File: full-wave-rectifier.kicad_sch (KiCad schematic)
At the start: 40 parts, among them J10 Control Right, J11 Main Right, J2 Input Ch1, J3 Input Ch2, J4 Output Ch1, J5 Output Ch2, J6 Ochd input, J8 Control Left, J9 Main Left, U2 TL074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

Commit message: Updated control panel
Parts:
- R10, R11, R12, R13, R14, R15, R16, R17, R18, R19, R20, R3, R4, R9: value 100k_TH0.125 -> 100k
- R21, R22: value 51k_TH0.125 -> 51k
- R5, R6, R7, R8: value 1k_TH0.125 -> 1k
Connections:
- net GND: now also J10.1 (Pin_1), J10.8 (Pin_8), J11.1 (Pin_1), J11.8 (Pin_8), J8.1 (Pin_1), J8.8 (Pin_8), J9.1 (Pin_1), J9.8 (Pin_8); no longer J10.4 (Pin_4), J10.6 (Pin_6), J11.4 (Pin_4), J11.6 (Pin_6), J8.4 (Pin_4), J8.6 (Pin_6), J9.4 (Pin_4), J9.6 (Pin_6)
- removed net AMP_CH1: AMP_CH1.1, J8.1 (Pin_1), J9.1 (Pin_1), R19.2, U4.7
- removed net AMP_CH2: AMP_CH2.1, J10.2 (Pin_2), J11.2 (Pin_2), R20.2, U4.8
- removed net INPUT_CH1: J8.7 (Pin_7), J9.7 (Pin_7), R5.2, U3.3 (+)
- removed net INPUT_CH2: J10.7 (Pin_7), J11.7 (Pin_7), R6.2, U3.12 (+)
- removed net OFFSET_CH1: J8.3 (Pin_3), J9.3 (Pin_3), OFFSET_CH1.1, U2.1, U2.2 (-)
- removed net OFFSET_CH2: J10.1 (Pin_1), J11.1 (Pin_1), OFFSET_CH2.1, U2.13 (-), U2.14
- removed net OUTPUT_CH1: J8.8 (Pin_8), J9.8 (Pin_8), R7.1, U3.6 (-), U3.7
- removed net OUTPUT_CH2: J10.8 (Pin_8), J11.8 (Pin_8), R8.1, U3.8, U3.9 (-)
- removed net SUM_CH1: J8.2 (Pin_2), J9.2 (Pin_2), R10.1, R9.2, U3.5 (+)
- removed net SUM_CH2: J10.3 (Pin_3), J11.3 (Pin_3), R11.2, R12.1, U3.10 (+)
- new net M_AMP_CH1: J9.3 (Pin_3), R19.2, U4.7
- new net M_AMP_CH2: J11.3 (Pin_3), R20.2, U4.8
- new net M_INPUT_CH1: J9.2 (Pin_2), U3.3 (+)
- new net M_INPUT_CH2: J11.2 (Pin_2), U3.12 (+)
- new net M_OFFSET_CH1: J9.6 (Pin_6), U2.1, U2.2 (-)
- new net M_OFFSET_CH2: J11.4 (Pin_4), U2.13 (-), U2.14
- new net M_OUTPUT_CH1: J9.7 (Pin_7), U3.6 (-), U3.7
- new net M_OUTPUT_CH2: J11.7 (Pin_7), U3.8, U3.9 (-)
- new net M_SUM_CH1: J9.4 (Pin_4), U3.5 (+)
- new net M_SUM_CH2: J11.6 (Pin_6), U3.10 (+)
- new net С_AMP_CH1: AMP_CH1.1, J8.3 (Pin_3)
- new net С_AMP_CH2: AMP_CH2.1, J10.3 (Pin_3)
- new net С_INPUT_CH1: J8.2 (Pin_2), R5.2
- new net С_INPUT_CH2: J10.2 (Pin_2), R6.2
- new net С_OFFSET_CH1: J8.6 (Pin_6), OFFSET_CH1.1
- new net С_OFFSET_CH2: J10.4 (Pin_4), OFFSET_CH2.1
- new net С_OUTPUT_CH1: J8.7 (Pin_7), R7.1
- new net С_OUTPUT_CH2: J10.7 (Pin_7), R8.1
- new net С_SUM_CH1: J8.4 (Pin_4), R10.1, R9.2
- new net С_SUM_CH2: J10.6 (Pin_6), R11.2, R12.1
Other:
- moved on the sheet: J10, J11, J6, J8, J9, U2B, U2C

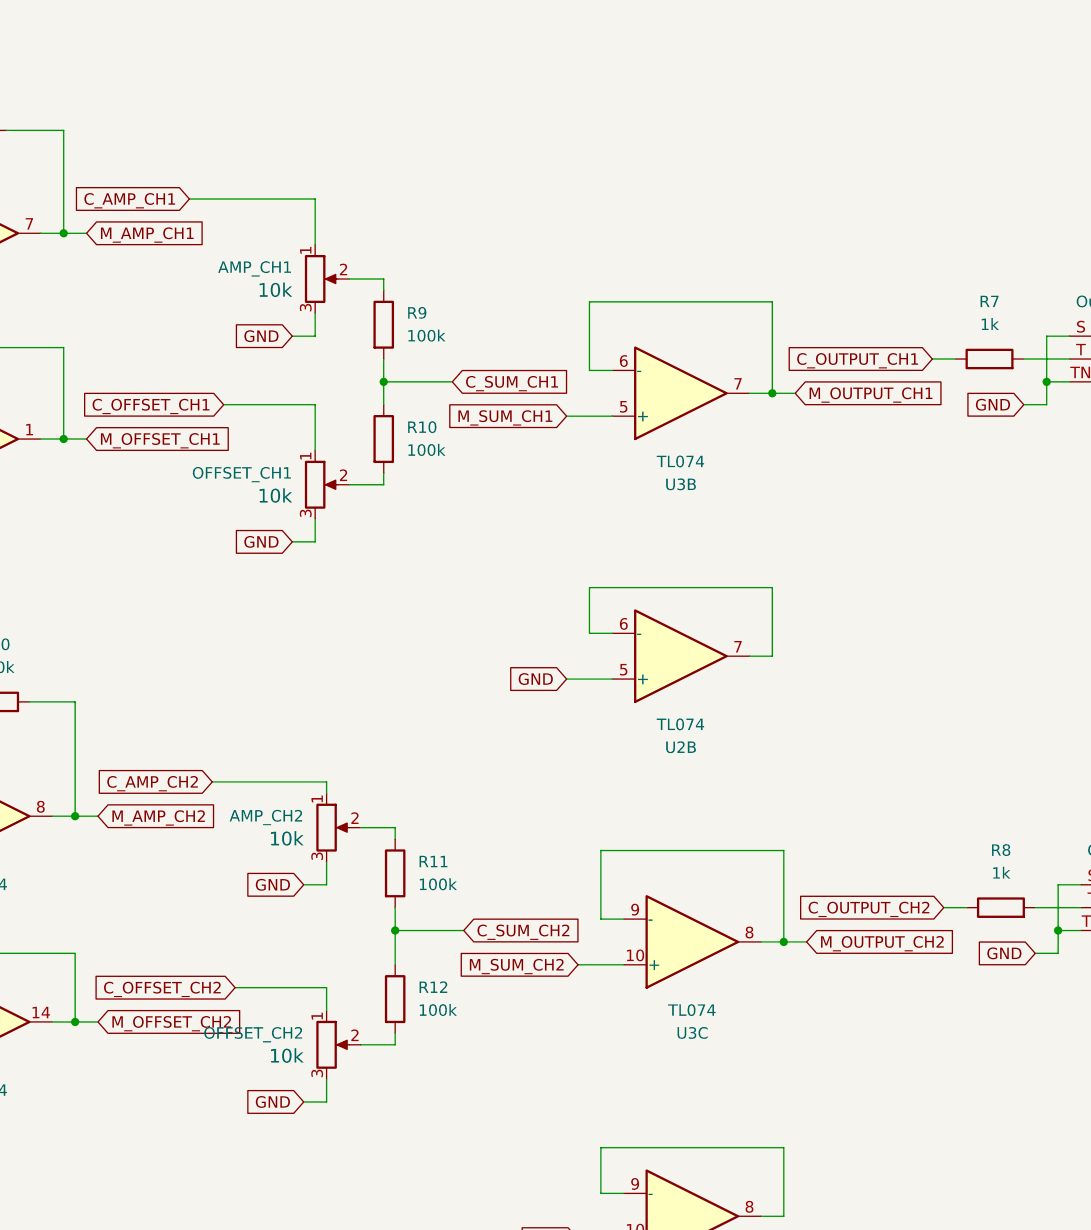
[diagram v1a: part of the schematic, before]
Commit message: fixed issue with Alpha pot legs
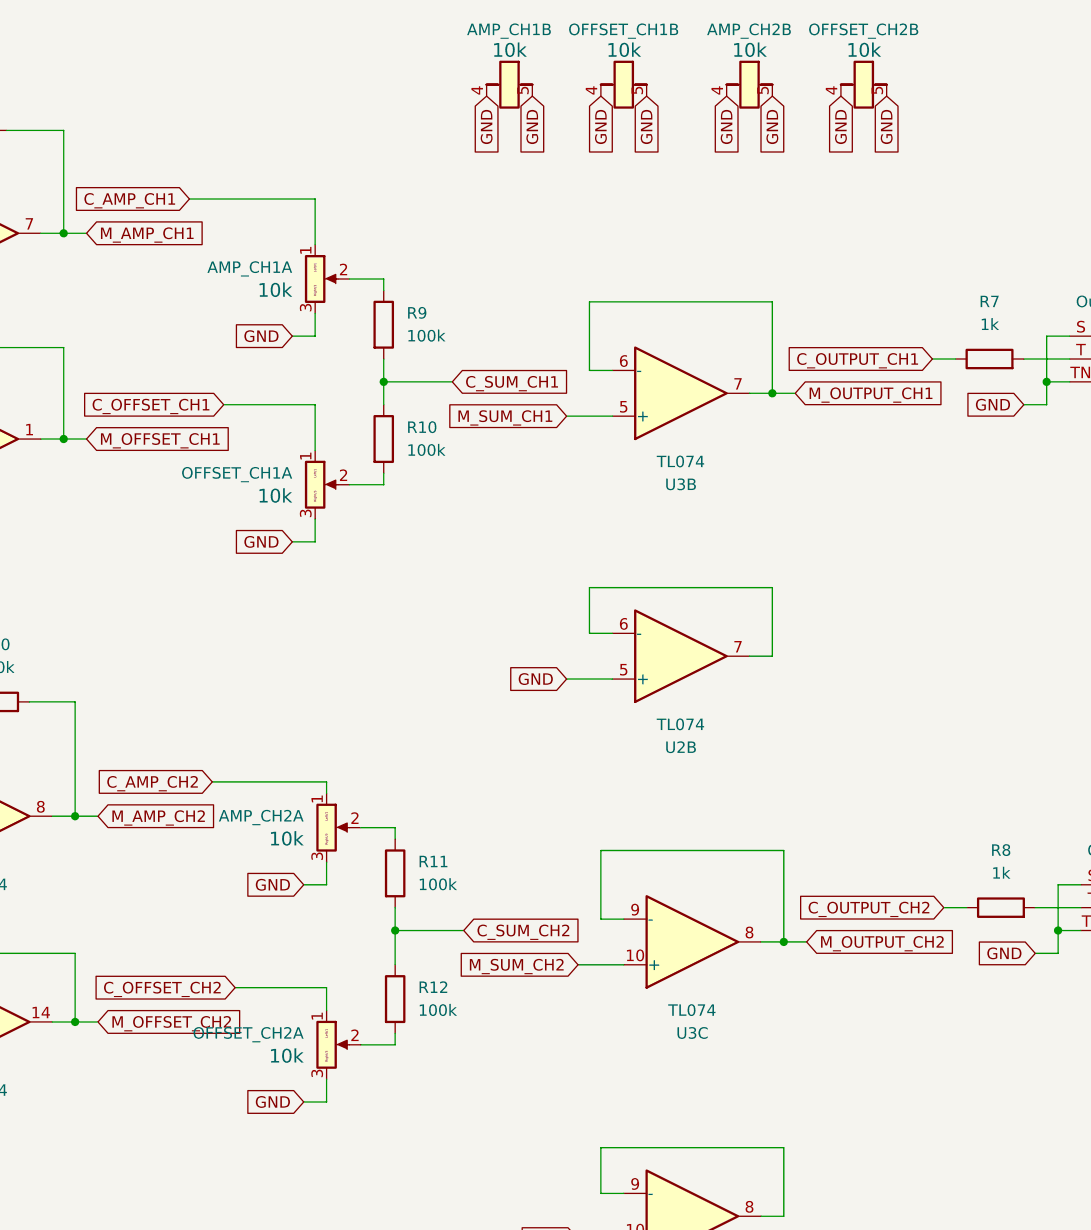
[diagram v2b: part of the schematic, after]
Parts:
- added unit 2 of AMP_CH1
- added unit 2 of AMP_CH2
- added unit 2 of OFFSET_CH1
- added unit 2 of OFFSET_CH2
- AMP_CH1, AMP_CH2, OFFSET_CH1, OFFSET_CH2: symbol Device:R_Potentiometer -> 4ms_Potentiometer:9mm_NoDet_10k_DShaft
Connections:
- net GND: now also AMP_CH1.4 (Tab1), AMP_CH1.5 (Tab2), AMP_CH2.4 (Tab1), AMP_CH2.5 (Tab2), OFFSET_CH1.4 (Tab1), OFFSET_CH1.5 (Tab2), OFFSET_CH2.4 (Tab1), OFFSET_CH2.5 (Tab2)

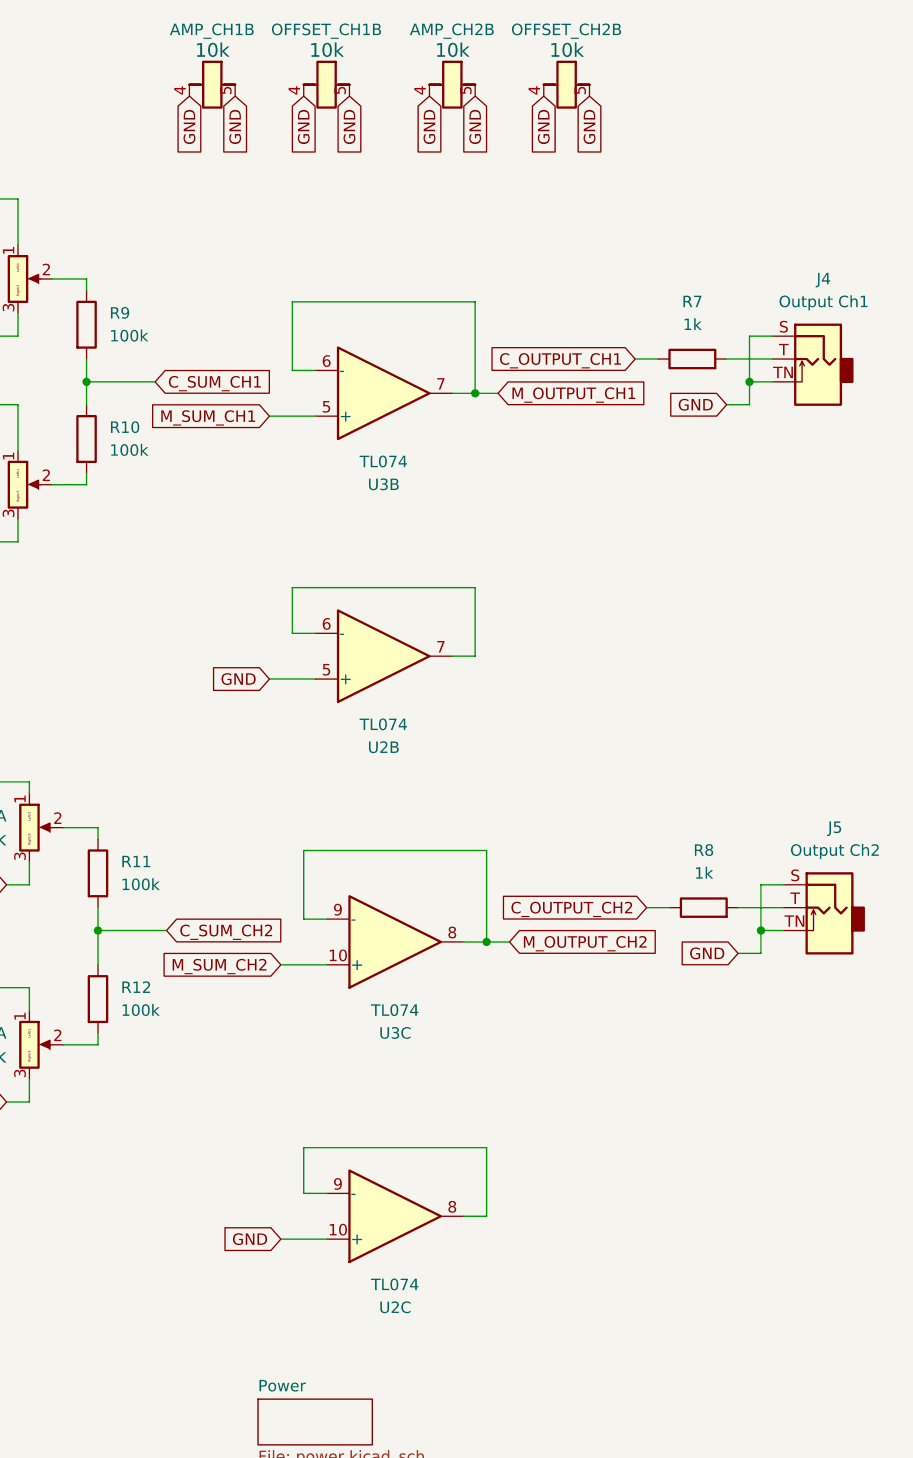
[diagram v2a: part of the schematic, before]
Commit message: Added test point
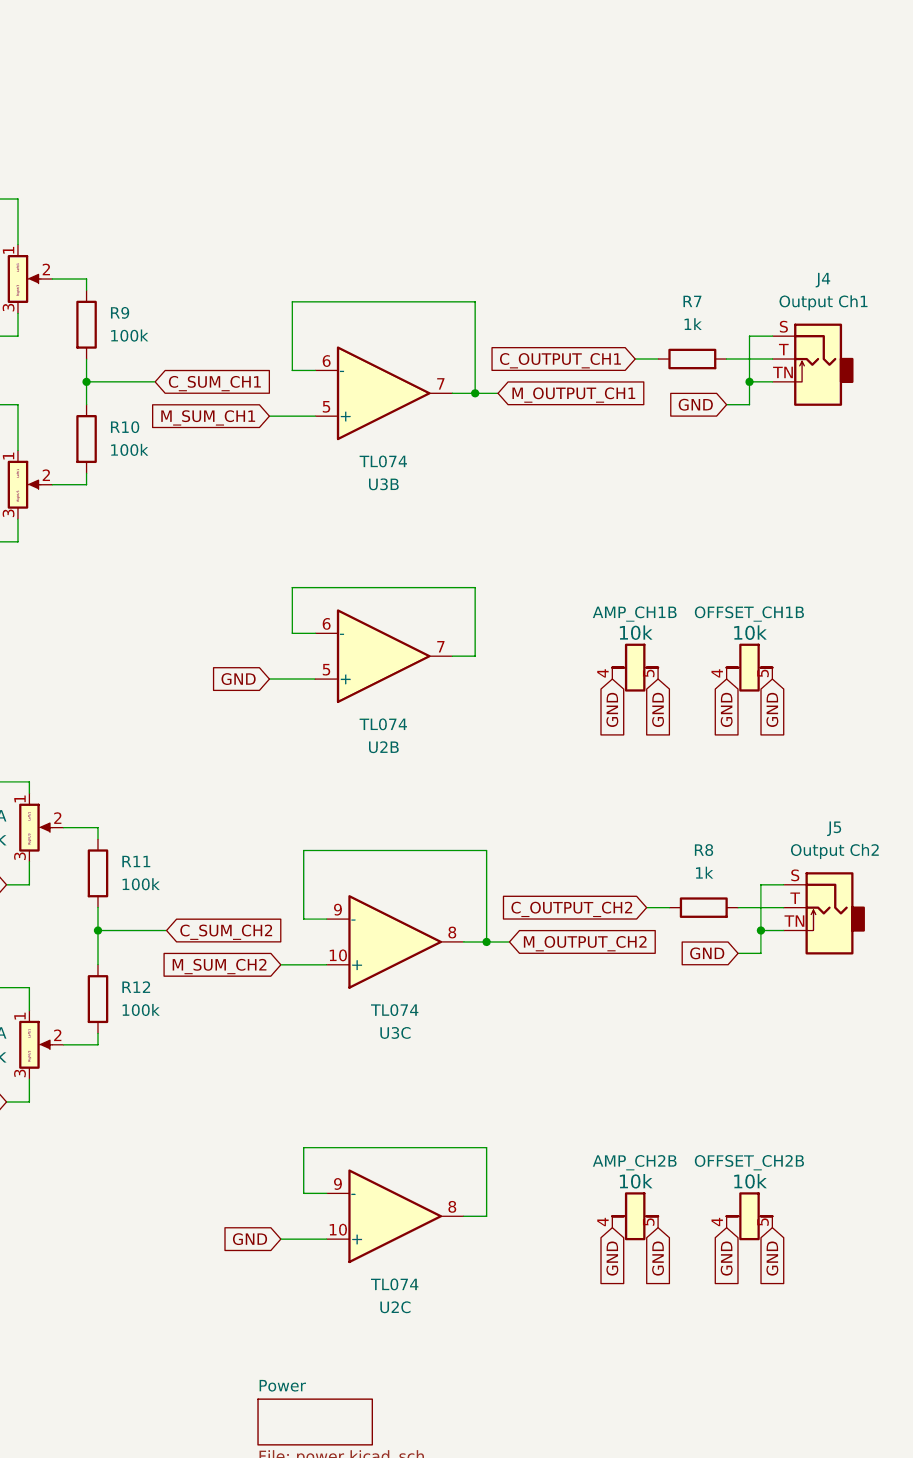
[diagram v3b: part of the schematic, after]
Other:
- moved on the sheet: AMP_CH1B, AMP_CH2B, OFFSET_CH1B, OFFSET_CH2B
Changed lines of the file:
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@@
 	(global_label "GND"
 		(shape input)
-		(at 223.52 25.4 270)
+		(at 270.51 90.17 270)
 		(fields_autoplaced yes)
 		(effects
@@
 		)
 		(property "Intersheetrefs" "${INTERSHEET_REFS}"
-			(at 223.52 32.2557 90)
+			(at 270.51 97.0257 90)
 			(effects
 				(font
@@
 	(global_label "GND"
 		(shape input)
-		(at 245.11 25.4 270)
+		(at 265.43 151.13 270)
 		(fields_autoplaced yes)
 		(effects
@@
 		)
 		(property "Intersheetrefs" "${INTERSHEET_REFS}"
-			(at 245.11 32.2557 90)
+			(at 265.43 157.9857 90)
 			(effects
 				(font
@@
 	(global_label "GND"
 		(shape input)
-		(at 232.41 25.4 270)
+		(at 252.73 151.13 270)
 		(fields_autoplaced yes)
 		(effects
@@
 		)
 		(property "Intersheetrefs" "${INTERSHEET_REFS}"
-			(at 232.41 32.2557 90)
+			(at 252.73 157.9857 90)
 			(effects
 				(font
@@
 	(global_label "GND"
 		(shape input)
-		(at 250.19 25.4 270)
+		(at 270.51 151.13 270)
 		(fields_autoplaced yes)
 		(effects
@@
 		)
 		(property "Intersheetrefs" "${INTERSHEET_REFS}"
-			(at 250.19 32.2557 90)
+			(at 270.51 157.9857 90)
 			(effects
 				(font
@@
 	(global_label "GND"
 		(shape input)
-		(at 210.82 25.4 270)
+		(at 257.81 90.17 270)
 		(fields_autoplaced yes)
 		(effects
@@
 		)
 		(property "Intersheetrefs" "${INTERSHEET_REFS}"
-			(at 210.82 32.2557 90)
+			(at 257.81 97.0257 90)
 			(effects
 				(font
@@
 	(global_label "GND"
 		(shape input)
-		(at 205.74 25.4 270)
+		(at 252.73 90.17 270)
 		(fields_autoplaced yes)
 		(effects
@@
 		)
 		(property "Intersheetrefs" "${INTERSHEET_REFS}"
-			(at 205.74 32.2557 90)
+			(at 252.73 97.0257 90)
 			(effects
 				(font
@@
 	(global_label "GND"
 		(shape input)
-		(at 218.44 25.4 270)
+		(at 265.43 90.17 270)
 		(fields_autoplaced yes)
 		(effects
@@
 		)
 		(property "Intersheetrefs" "${INTERSHEET_REFS}"
-			(at 218.44 32.2557 90)
+			(at 265.43 97.0257 90)
 			(effects
 				(font
@@
 	(global_label "GND"
 		(shape input)
-		(at 237.49 25.4 270)
+		(at 257.81 151.13 270)
 		(fields_autoplaced yes)
 		(effects
@@
 		)
 		(property "Intersheetrefs" "${INTERSHEET_REFS}"
-			(at 237.49 32.2557 90)
+			(at 257.81 157.9857 90)
 			(effects
 				(font
@@
 	(symbol
 		(lib_id "4ms_Potentiometer:9mm_NoDet_10k_DShaft")
-		(at 247.65 24.13 0)
+		(at 267.97 149.86 0)
 		(unit 2)
 		(exclude_from_sim no)
@@
 		(dnp no)
 		(property "Reference" "OFFSET_CH2"
-			(at 247.65 18.034 0)
+			(at 267.97 143.764 0)
 			(effects
 				(font
@@
 		)
 		(property "Value" "10k"
-			(at 247.65 17.78 0)
+			(at 267.97 143.51 0)
 			(effects
 				(font
@@
 		)
 		(property "Footprint" "Eurorack:Pot_Alpha_9mm"
-			(at 247.65 24.13 0)
+			(at 267.97 149.86 0)
 			(effects
 				(font
@@
 		)
 		(property "Datasheet" "~"
-			(at 247.65 24.13 0)
+			(at 267.97 149.86 0)
 			(effects
 				(font
@@
 		)
 		(property "Description" "10k Linear, 9mm pot, No Detent, D-Shaft"
-			(at 247.65 24.13 0)
+			(at 267.97 149.86 0)
 			(effects
 				(font
@@
 		)
 		(property "Specifications" "10k Linear, 9mm pot, No Detent, D-Shaft"
-			(at 245.11 32.004 0)
+			(at 265.43 157.734 0)
 			(effects
 				(font
@@
 		)
 		(property "Manufacturer" "Alpha Taiwan "
-			(at 245.11 33.528 0)
+			(at 265.43 159.258 0)
 			(effects
 				(font
@@
 		)
 		(property "Part Number" "RV09BCF-40-25F-B10K-007 "
-			(at 245.11 35.052 0)
+			(at 265.43 160.782 0)
 			(effects
 				(font
@@
 		)
 		(property "Display" "10k"
-			(at 247.65 20.32 0)
+			(at 267.97 146.05 0)
 			(effects
 				(font
@@
 		)
 		(property "Production Stage" "C"
-			(at 247.4722 37.1094 0)
+			(at 267.7922 162.8394 0)
 			(effects
 				(font
@@
 	(symbol
 		(lib_id "4ms_Potentiometer:9mm_NoDet_10k_DShaft")
-		(at 220.98 24.13 0)
+		(at 267.97 88.9 0)
 		(unit 2)
 		(exclude_from_sim no)
@@
 		(dnp no)
 		(property "Reference" "OFFSET_CH1"
-			(at 220.98 18.034 0)
+			(at 267.97 82.804 0)
 			(effects
 				(font
@@
 		)
 		(property "Value" "10k"
-			(at 220.98 17.78 0)
+			(at 267.97 82.55 0)
 			(effects
 				(font
@@
 		)
 		(property "Footprint" "Eurorack:Pot_Alpha_9mm"
-			(at 220.98 24.13 0)
+			(at 267.97 88.9 0)
 			(effects
 				(font
@@
 		)
 		(property "Datasheet" "~"
-			(at 220.98 24.13 0)
+			(at 267.97 88.9 0)
 			(effects
 				(font
@@
 		)
 		(property "Description" "10k Linear, 9mm pot, No Detent, D-Shaft"
-			(at 220.98 24.13 0)
+			(at 267.97 88.9 0)
 			(effects
 				(font
@@
 		)
 		(property "Specifications" "10k Linear, 9mm pot, No Detent, D-Shaft"
-			(at 218.44 32.004 0)
+			(at 265.43 96.774 0)
 			(effects
 				(font
@@
 		)
 		(property "Manufacturer" "Alpha Taiwan "
-			(at 218.44 33.528 0)
+			(at 265.43 98.298 0)
 			(effects
 				(font
@@
 		)
 		(property "Part Number" "RV09BCF-40-25F-B10K-007 "
-			(at 218.44 35.052 0)
+			(at 265.43 99.822 0)
 			(effects
 				(font
@@
 		)
 		(property "Display" "10k"
-			(at 220.98 20.32 0)
+			(at 267.97 85.09 0)
 			(effects
 				(font
@@
 		)
 		(property "Production Stage" "C"
-			(at 220.8022 37.1094 0)
+			(at 267.7922 101.8794 0)
 			(effects
 				(font
@@
 	(symbol
 		(lib_id "4ms_Potentiometer:9mm_NoDet_10k_DShaft")
-		(at 208.28 24.13 0)
+		(at 255.27 88.9 0)
 		(unit 2)
 		(exclude_from_sim no)
@@
 		(dnp no)
 		(property "Reference" "AMP_CH1"
-			(at 208.28 18.034 0)
+			(at 255.27 82.804 0)
 			(effects
 				(font
@@
 		)
 		(property "Value" "10k"
-			(at 208.28 17.78 0)
+			(at 255.27 82.55 0)
 			(effects
 				(font
@@
 		)
 		(property "Footprint" "Eurorack:Pot_Alpha_9mm"
-			(at 208.28 24.13 0)
+			(at 255.27 88.9 0)
 			(effects
 				(font
@@
 		)
 		(property "Datasheet" "~"
-			(at 208.28 24.13 0)
+			(at 255.27 88.9 0)
 			(effects
 				(font
@@
 		)
 		(property "Description" "10k Linear, 9mm pot, No Detent, D-Shaft"
-			(at 208.28 24.13 0)
+			(at 255.27 88.9 0)
 			(effects
 				(font
@@
 		)
 		(property "Specifications" "10k Linear, 9mm pot, No Detent, D-Shaft"
-			(at 205.74 32.004 0)
+			(at 252.73 96.774 0)
 			(effects
 				(font
@@
 		)
 		(property "Manufacturer" "Alpha Taiwan "
-			(at 205.74 33.528 0)
+			(at 252.73 98.298 0)
 			(effects
 				(font
@@
 		)
 		(property "Part Number" "RV09BCF-40-25F-B10K-007 "
-			(at 205.74 35.052 0)
+			(at 252.73 99.822 0)
 			(effects
 				(font
@@
 		)
 		(property "Display" "10k"
-			(at 208.28 20.32 0)
+			(at 255.27 85.09 0)
 			(effects
 				(font
@@
 		)
 		(property "Production Stage" "C"
-			(at 208.1022 37.1094 0)
+			(at 255.0922 101.8794 0)
 			(effects
 				(font
@@
 	(symbol
 		(lib_id "4ms_Potentiometer:9mm_NoDet_10k_DShaft")
-		(at 234.95 24.13 0)
+		(at 255.27 149.86 0)
 		(unit 2)
 		(exclude_from_sim no)
@@
 		(dnp no)
 		(property "Reference" "AMP_CH2"
-			(at 234.95 18.034 0)
+			(at 255.27 143.764 0)
 			(effects
 				(font
@@
 		)
 		(property "Value" "10k"
-			(at 234.95 17.78 0)
+			(at 255.27 143.51 0)
 			(effects
 				(font
@@
 		)
 		(property "Footprint" "Eurorack:Pot_Alpha_9mm"
-			(at 234.95 24.13 0)
+			(at 255.27 149.86 0)
 			(effects
 				(font
@@
 		)
 		(property "Datasheet" "~"
-			(at 234.95 24.13 0)
+			(at 255.27 149.86 0)
 			(effects
 				(font
@@
 		)
 		(property "Description" "10k Linear, 9mm pot, No Detent, D-Shaft"
-			(at 234.95 24.13 0)
+			(at 255.27 149.86 0)
 			(effects
 				(font
@@
 		)
 		(property "Specifications" "10k Linear, 9mm pot, No Detent, D-Shaft"
-			(at 232.41 32.004 0)
+			(at 252.73 157.734 0)
 			(effects
 				(font
@@
 		)
 		(property "Manufacturer" "Alpha Taiwan "
-			(at 232.41 33.528 0)
+			(at 252.73 159.258 0)
 			(effects
 				(font
@@
 		)
 		(property "Part Number" "RV09BCF-40-25F-B10K-007 "
-			(at 232.41 35.052 0)
+			(at 252.73 160.782 0)
 			(effects
 				(font
@@
 		)
 		(property "Display" "10k"
-			(at 234.95 20.32 0)
+			(at 255.27 146.05 0)
 			(effects
 				(font
@@
 		)
 		(property "Production Stage" "C"
-			(at 234.7722 37.1094 0)
+			(at 255.0922 162.8394 0)
 			(effects
 				(font

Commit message: save chages
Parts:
- added D22, D23, D24, D25: D_TVS, Diode_SMD:D_SOD-323_HandSoldering, symbol Device:D_TVS
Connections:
- net GND: now also D22.2 (A2), D23.2 (A2), D24.2 (A2), D25.2 (A2); no longer J4.TN, J5.TN
- net at J5.T, R8.2: now also D25.1 (A1)
- net at J3.T, R4.1, R6.1: now also D23.1 (A1)
- net at J2.T, R3.1, R5.1: now also D22.1 (A1)
- net at J4.T, R7.2: now also D24.1 (A1)
- no-connect marks 0 -> 2
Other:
- moved on the sheet: R3
